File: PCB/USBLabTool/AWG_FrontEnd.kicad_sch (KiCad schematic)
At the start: 32 parts, among them J17 2x01, U10 Opamp_Quad, U11 DG403, U9 Opamp_Quad

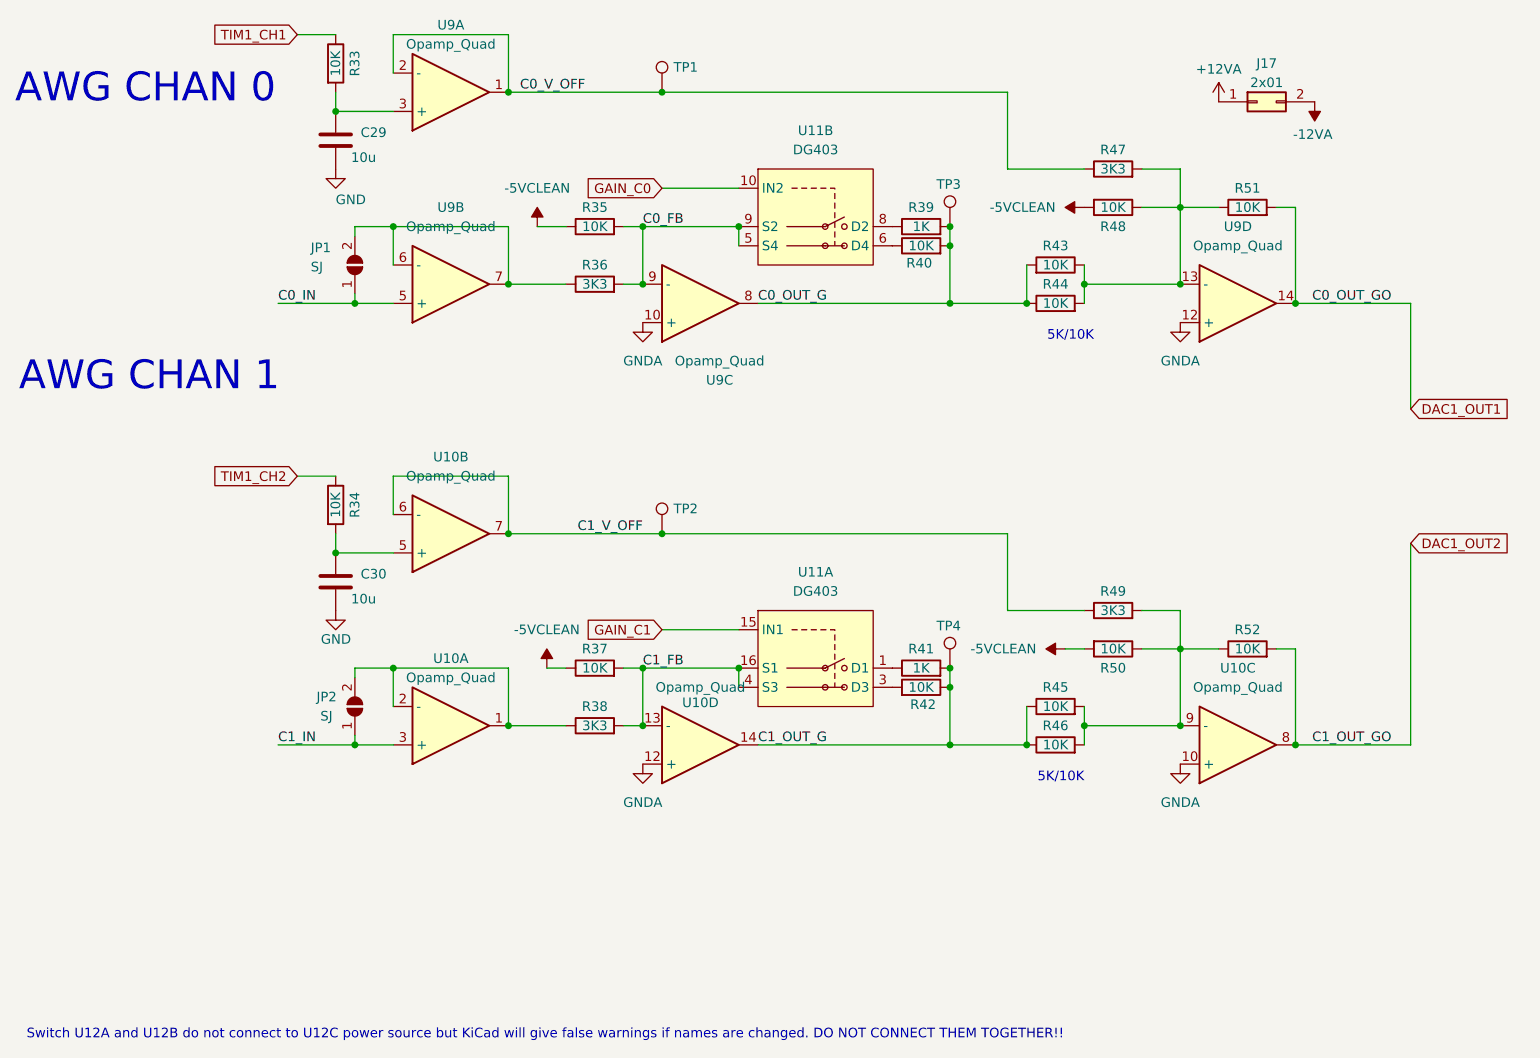
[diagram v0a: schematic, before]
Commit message: fixed AWG pins to MCU
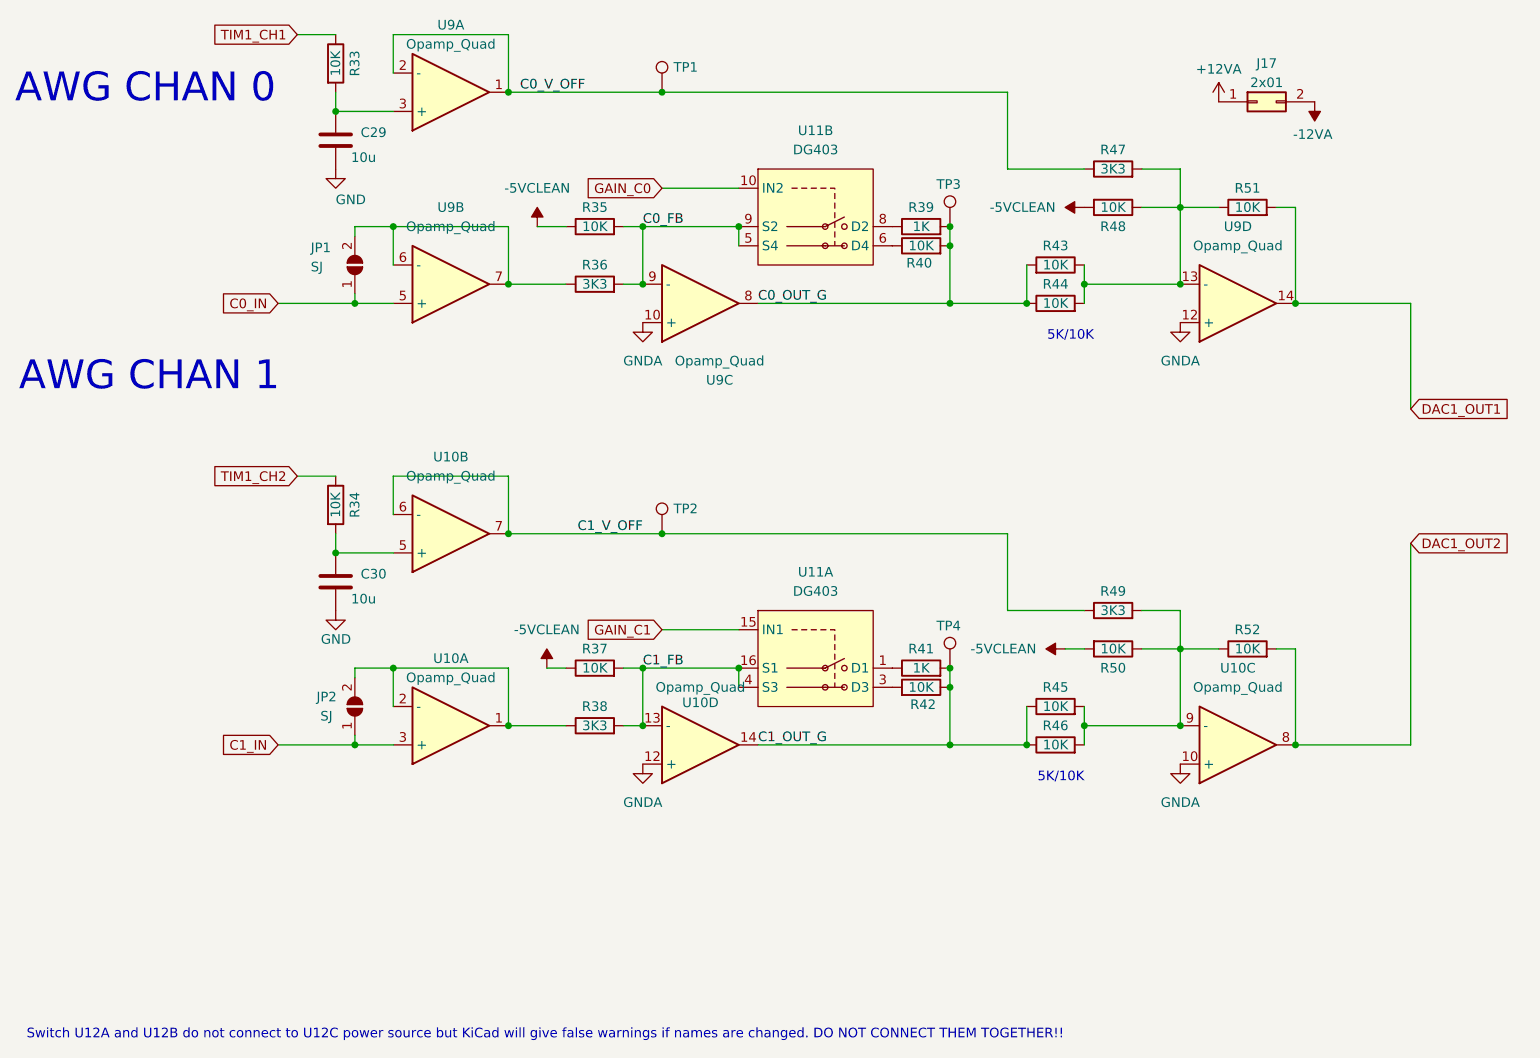
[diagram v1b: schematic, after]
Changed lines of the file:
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@@
-		)
-	)
-	(label "C1_OUT_GO"
-		(at 195.58 114.3 180)
-		(effects
-			(font
-				(size 1.27 1.27)
-			)
-			(justify right bottom)
-		)
-	)
-	(label "C0_OUT_GO"
-		(at 195.58 55.88 180)
-		(effects
-			(font
-				(size 1.27 1.27)
-			)
-			(justify right bottom)
-		)
-	)
-	(label "C1_IN"
-		(at 48.26 114.3 0)
-		(effects
-			(font
-				(size 1.27 1.27)
-			)
-			(justify left bottom)
 		)
 	)
@@
 	(label "C1_OUT_G"
 		(at 111.76 114.3 0)
-		(effects
-			(font
-				(size 1.27 1.27)
-			)
-			(justify left bottom)
-		)
-	)
-	(label "C0_IN"
-		(at 48.26 55.88 0)
 		(effects
 			(font
@@
 				)
 				(justify left)
+				(hide yes)
+			)
+		)
+	)
+	(global_label "C1_IN"
+		(shape input)
+		(at 48.26 114.3 180)
+		(fields_autoplaced yes)
+		(effects
+			(font
+				(size 1.27 1.27)
+			)
+			(justify right)
+		)
+		(property "Intersheetrefs" "${INTERSHEET_REFS}"
+			(at 39.8924 114.3 0)
+			(effects
+				(font
+					(size 1.27 1.27)
+				)
+				(justify right)
 				(hide yes)
 			)
@@
 			(effects
 				(font
+					(size 1.27 1.27)
+				)
+				(justify right)
+				(hide yes)
+			)
+		)
+	)
+	(global_label "C0_IN"
+		(shape input)
+		(at 48.26 55.88 180)
+		(fields_autoplaced yes)
+		(effects
+			(font
+				(size 1.27 1.27)
+			)
+			(justify right)
+		)
+		(property "Intersheetrefs" "${INTERSHEET_REFS}"
+			(at 39.8924 55.88 0)
+			(effects
+				(font

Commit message: just add a note
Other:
- note added: "may not needed in final version"
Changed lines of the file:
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@@
+		)
+	)
+	(text "may not needed in final version"
+		(exclude_from_sim no)
+		(at 181.864 20.574 0)
+		(effects
+			(font
+				(size 1.27 1.27)
+			)
 		)
 	)

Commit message: change USB footprint, fix some warnings and problems
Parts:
- JP1, JP2: footprint Jumper:SolderJumper-2_P1.3mm_Open_TrianglePad1.0x1.5mm -> Jumper:SolderJumper-2_P1.3mm_Open_RoundedPad1.0x1.5mm
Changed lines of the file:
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@@
 			)
 		)
-		(property "Footprint" "Jumper:SolderJumper-2_P1.3mm_Open_TrianglePad1.0x1.5mm"
+		(property "Footprint" "Jumper:SolderJumper-2_P1.3mm_Open_RoundedPad1.0x1.5mm"
 			(at 58.42 109.22 0)
 			(effects
@@
 			)
 		)
-		(property "Footprint" "Jumper:SolderJumper-2_P1.3mm_Open_TrianglePad1.0x1.5mm"
+		(property "Footprint" "Jumper:SolderJumper-2_P1.3mm_Open_RoundedPad1.0x1.5mm"
 			(at 58.42 50.8 0)
 			(effects

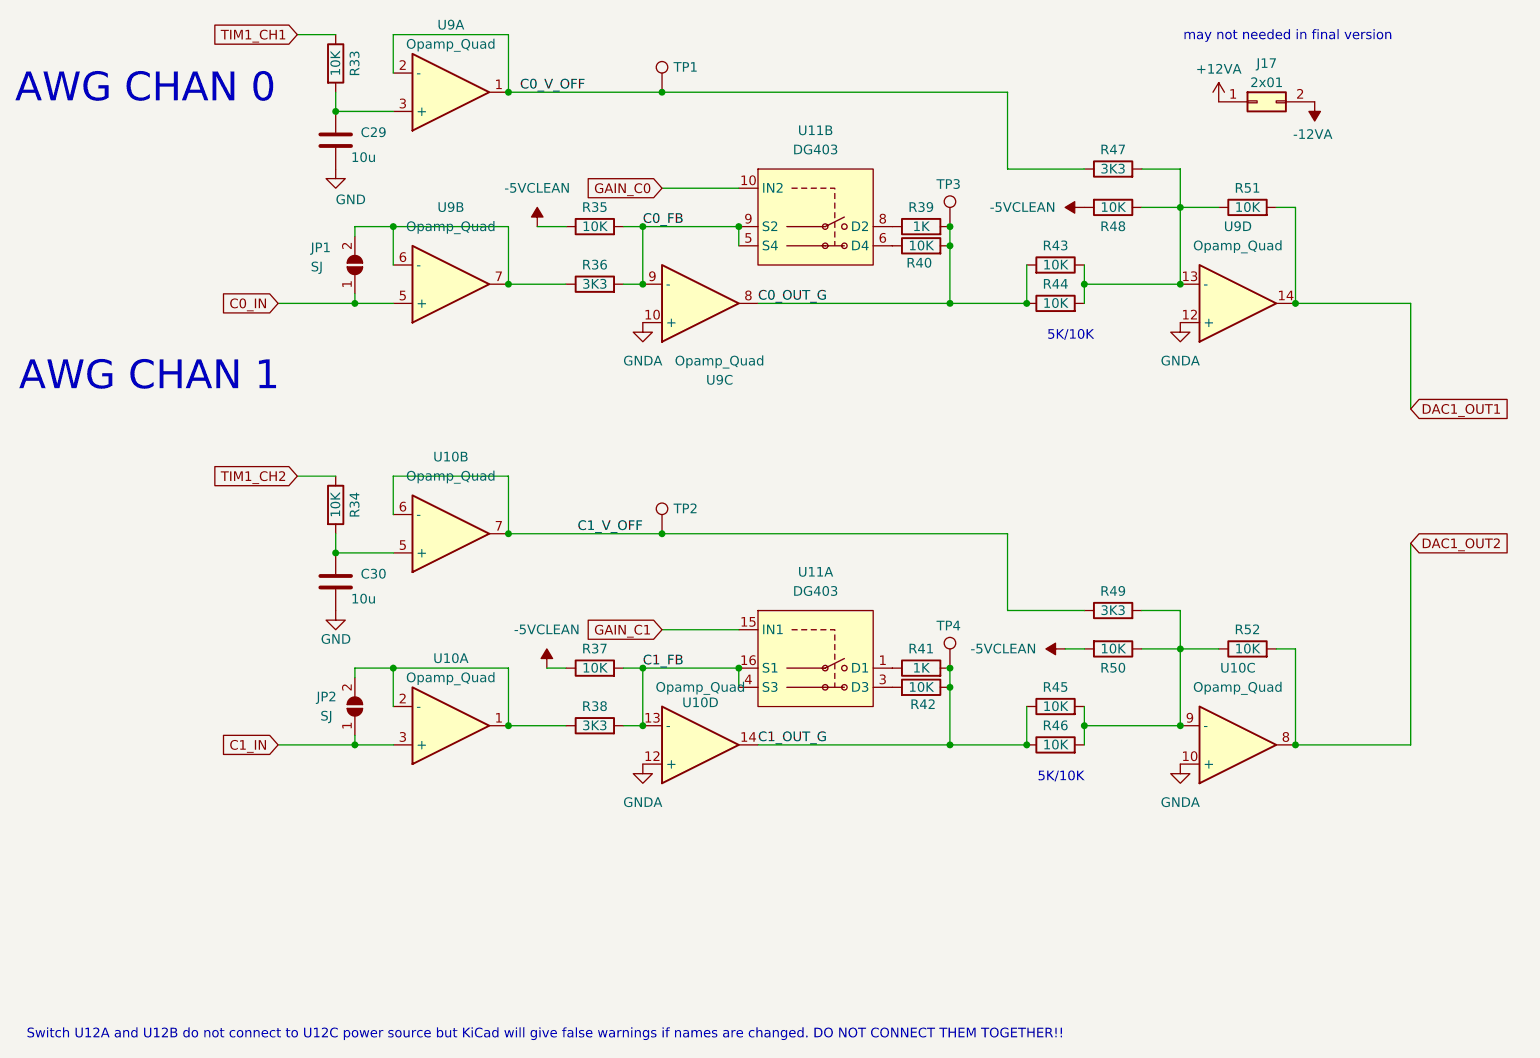
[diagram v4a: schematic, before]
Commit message: Resolved DRC/ERC errors in PCB and schematic
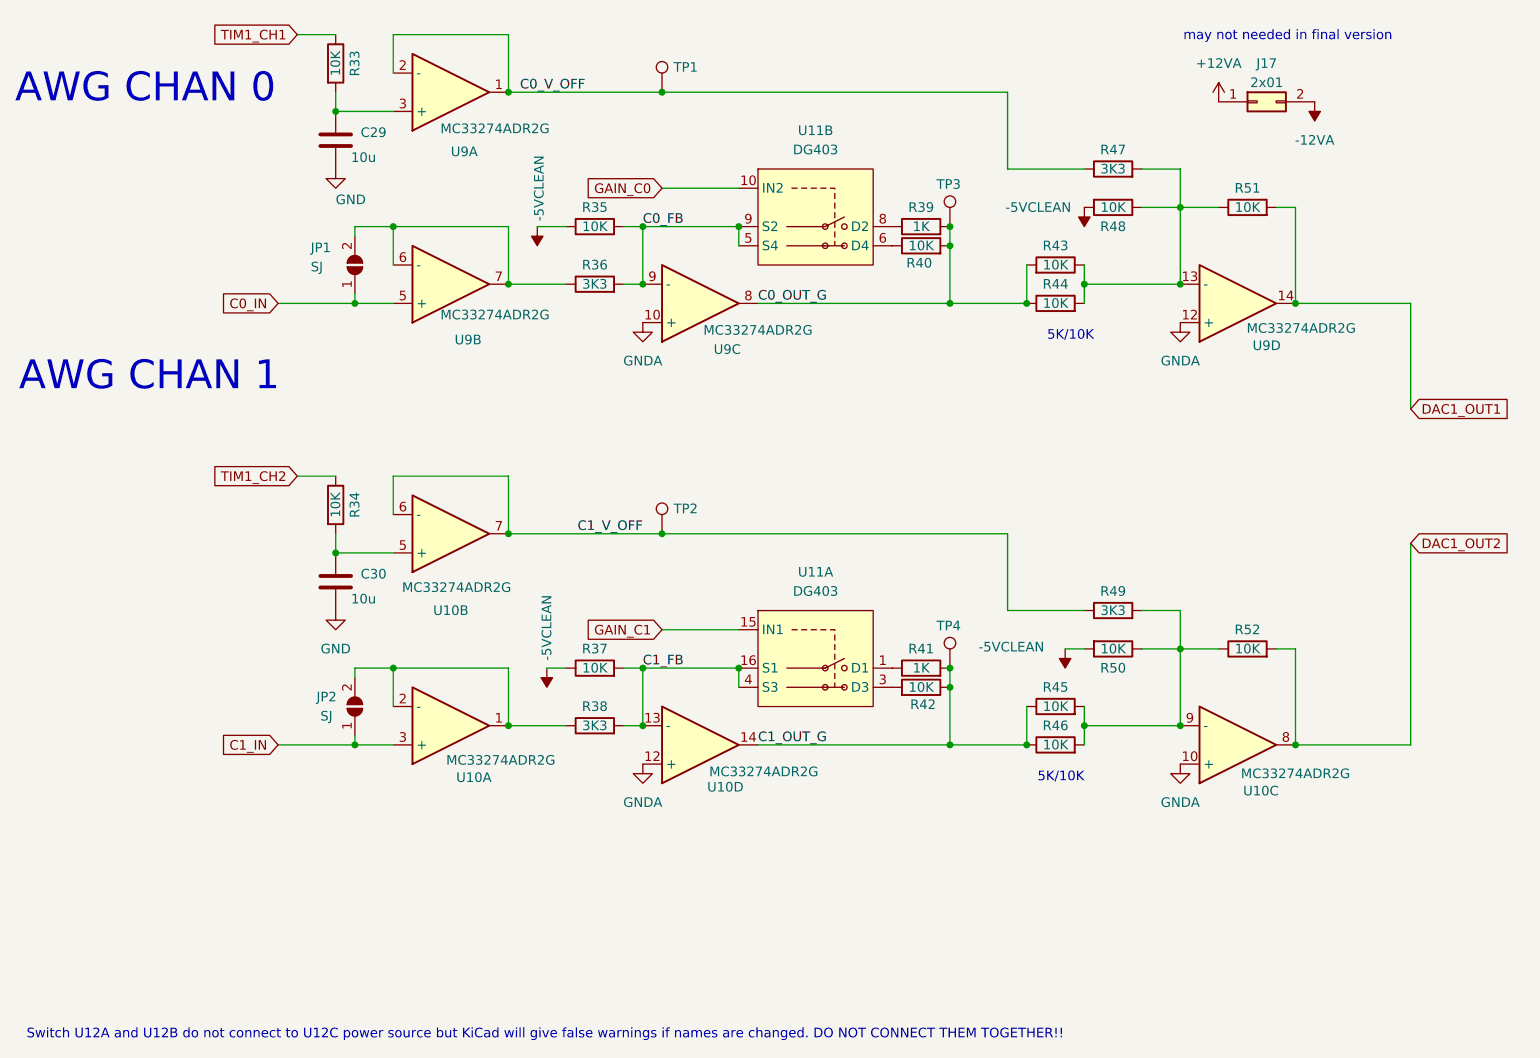
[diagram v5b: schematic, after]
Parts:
- removed U11: DG403, Package_SO:TSSOP-16-1EP_4.4x5mm_P0.65mm, symbol awg_lib:DG403
- added U11: DG403, Package_SO:TSSOP-16_4.4x5mm_P0.65mm, symbol USBLabTool:DG403
- U10: value Opamp_Quad -> MC33274ADR2G
- U9: value Opamp_Quad -> MC33274ADR2G; BUY https://www.digikey.com/en/products/detail/onsemi/MC33274AD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 -> (none)
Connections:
- net C0_FB: now also U11.5 (S4), U11.9 (S2)
- net C1_FB: now also U11.16 (S1), U11.4 (S3)
- net GAIN_C0: now also U11.10 (IN2)
- net GAIN_C1: now also U11.15 (IN1)
- net at R41.1: now also U11.1 (D1)
- net at R42.2: now also U11.3 (D3)
- net at R40.1: now also U11.6 (D4)
- net at R39.1: now also U11.8 (D2)
